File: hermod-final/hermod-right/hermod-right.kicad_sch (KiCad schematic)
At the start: 40 parts, among them J1 USB_C_Receptacle_USB2.0, J2 Conn_01x05, J3 USB_C_Receptacle_USB2.0, Q1 AO3401A, Q2 MMUN2233LT1G, U1 STM32F072CBT6, U2 PRTR5V0U2X, U3 XC6206PxxxMR-Regulator_Linear, U4 CR2013-MI2120, U5 TXB0101

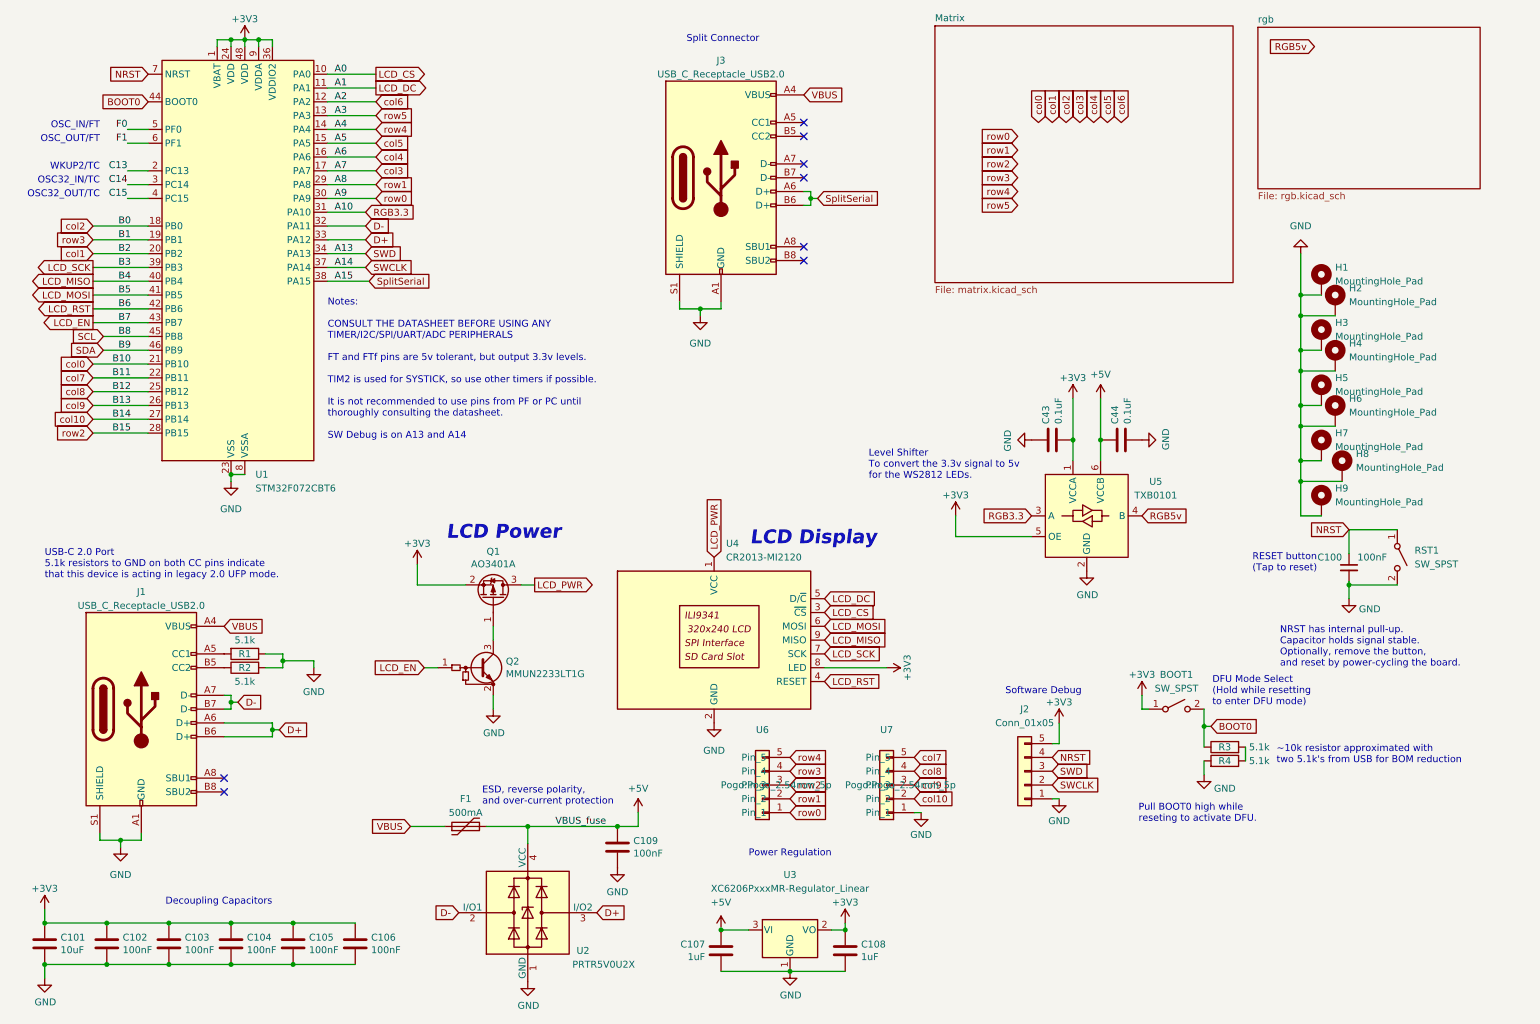
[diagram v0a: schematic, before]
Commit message: Finished hermod designs
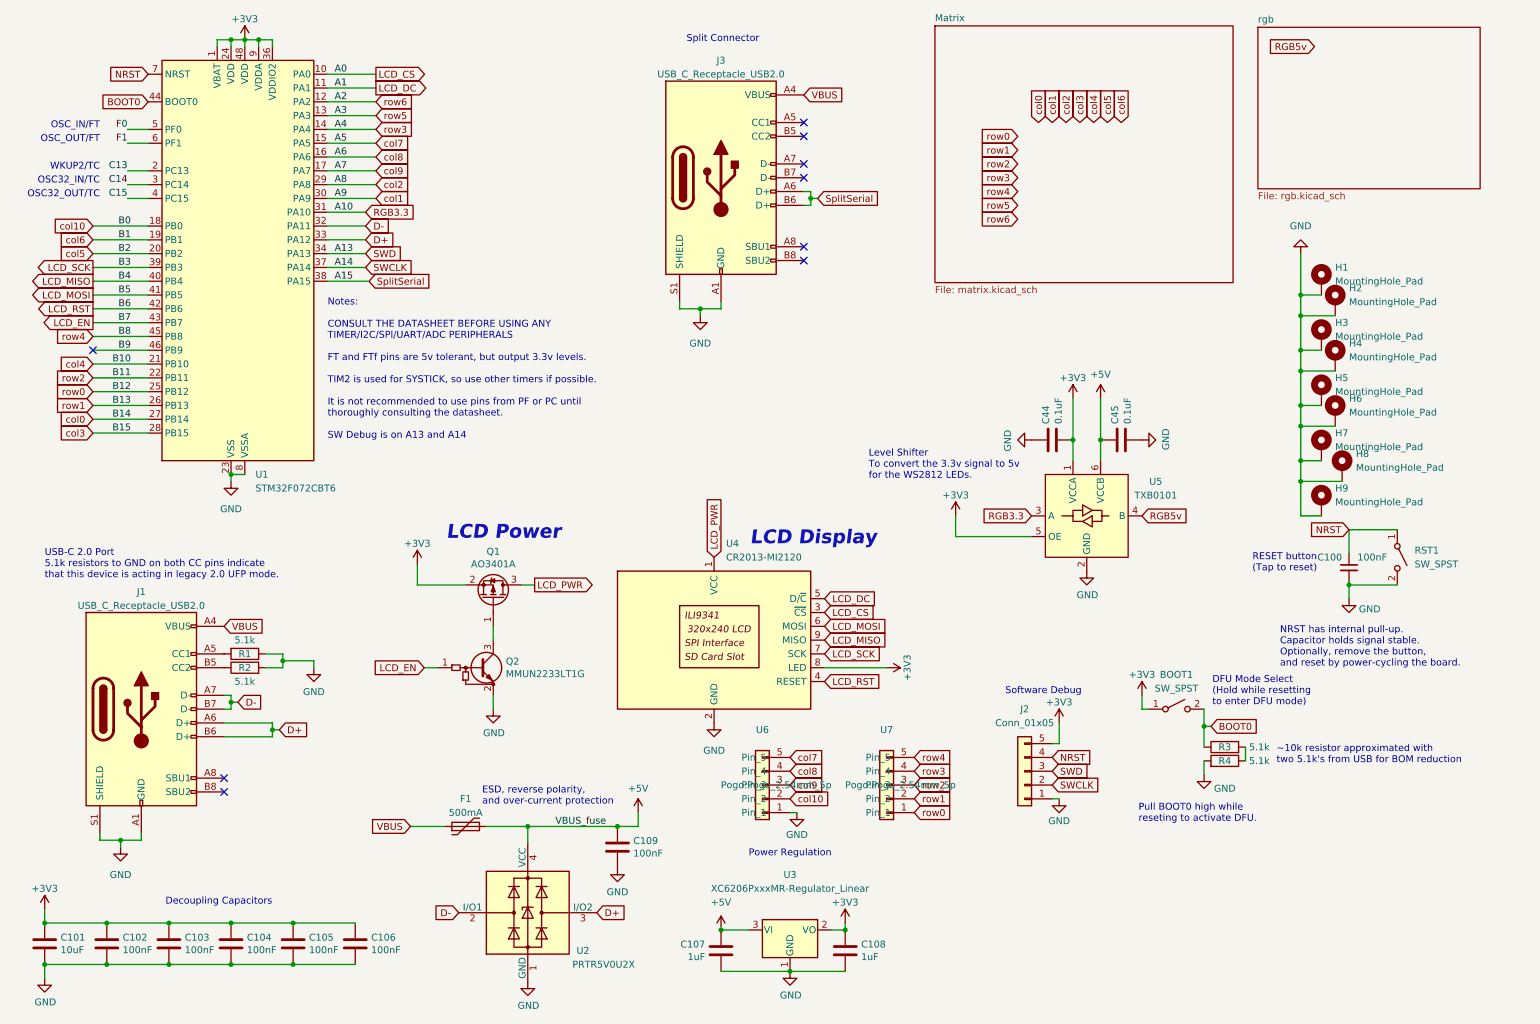
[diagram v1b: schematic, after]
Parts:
- renumbered C43 to C44, C44 to C45
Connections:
- net SCL is gone; now on net row4: U1.45 (PB8)
- net GND: now also U6.1 (Pin_1); no longer U7.1 (Pin_1)
- net col0: now also U1.27 (PB14); no longer U1.21 (PB10)
- net col1: now also U1.30 (PA9); no longer U1.20 (PB2)
- net col10: now also U1.18 (PB0), U6.2 (Pin_2); no longer U1.27 (PB14), U7.2 (Pin_2)
- net col2: now also U1.29 (PA8); no longer U1.18 (PB0)
- net col3: now also U1.28 (PB15); no longer U1.17 (PA7)
- net col4: now also U1.21 (PB10); no longer U1.16 (PA6)
- net col5: now also U1.20 (PB2); no longer U1.15 (PA5)
- net col6: now also U1.19 (PB1); no longer U1.12 (PA2)
- net col7: now also U1.15 (PA5), U6.5 (Pin_5); no longer U1.22 (PB11), U7.5 (Pin_5)
- net col8: now also U1.16 (PA6), U6.4 (Pin_4); no longer U1.25 (PB12), U7.4 (Pin_4)
- net col9: now also U1.17 (PA7), U6.3 (Pin_3); no longer U1.26 (PB13), U7.3 (Pin_3)
- net row0: now also U1.25 (PB12), U7.1 (Pin_1); no longer U1.30 (PA9), U6.1 (Pin_1)
- net row1: now also U1.26 (PB13), U7.2 (Pin_2); no longer U1.29 (PA8), U6.2 (Pin_2)
- net row2: now also U1.22 (PB11), U7.3 (Pin_3); no longer U1.28 (PB15), U6.3 (Pin_3)
- net row3: now also U1.14 (PA4), U7.4 (Pin_4); no longer U1.19 (PB1), U6.4 (Pin_4)
- net row4: now also U7.5 (Pin_5); no longer U1.14 (PA4), U6.5 (Pin_5)
- net SDA renamed B9
- new net row6: U1.12 (PA2)
- no-connect marks 8 -> 9
